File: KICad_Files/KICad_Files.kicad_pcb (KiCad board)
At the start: 2 copper layers, 30 x 34 mm, 42 parts, among them J1 Conn_01x03_MountingPin, J2 Conn_01x03_MountingPin, J3 Conn_01x03_MountingPin, J4 USB_C_Receptacle_USB2.0_14P, J5 Conn_01x06, J6 Conn_01x06, J7 Conn_01x03_Pin, J8 Conn_01x03_Pin, SW1 Reset, SW2 Boot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

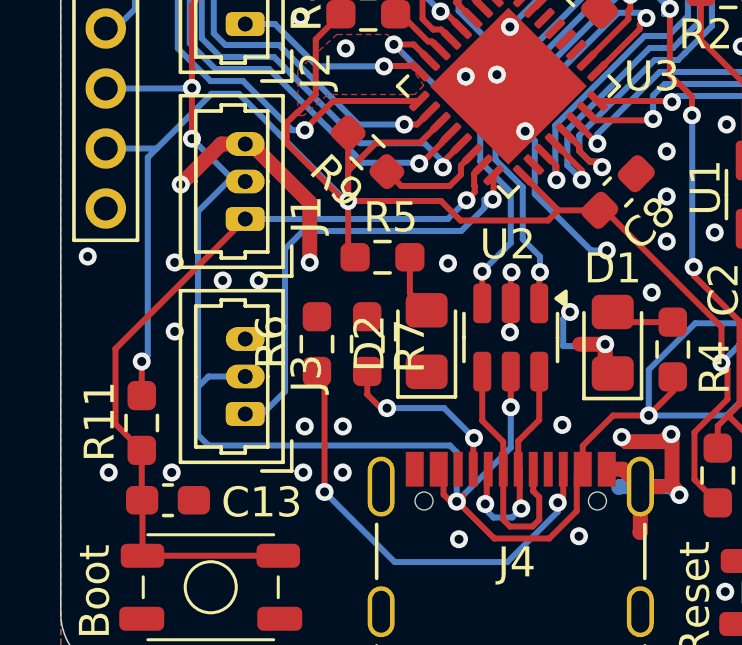
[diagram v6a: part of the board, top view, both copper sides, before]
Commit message: Properly named all I/O Pins/ Power Pins on the Back fixed some minor errors where the silkscreen wasnt aligned properly
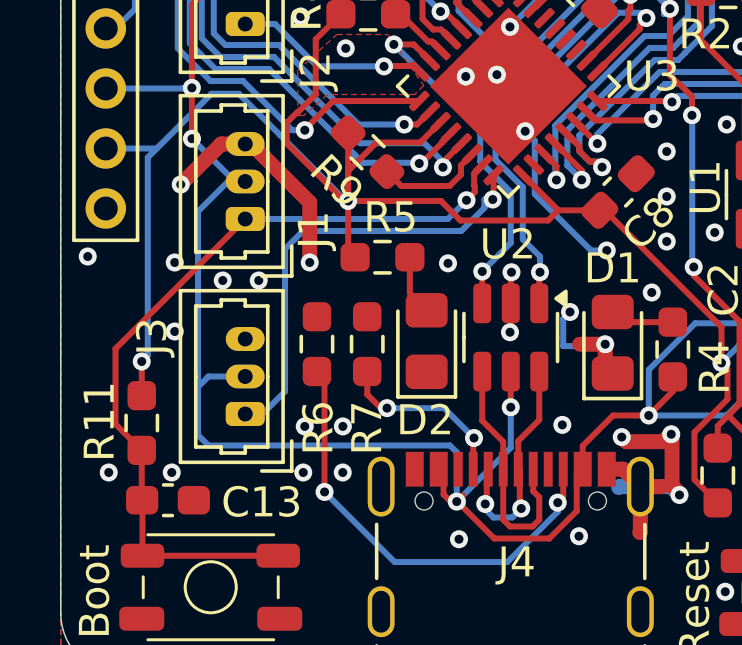
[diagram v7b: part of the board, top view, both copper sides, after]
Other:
- board text added: "3.3V"
- board text added: "GPIO0/4"
- board text added: "GPIO1/5"
- board text added: "GPIO12/19"
- board text added: "GPIO13/20"
- board text added: "GPIO14/21"
- board text added: "GPIO15/22"
- board text added: "GPIO16/23"
- board text added: "GPIO17/24"
- board text added: "GPIO3/8"
- board text added: "GPIO5/10"
- board text added: "GPIO6/12"
- board text added: "GPIO7/13"
- board text added: "GPIO9/15"
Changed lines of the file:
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@@
 		(tags "resistor handsolder")
 		(property "Reference" "R7"
-			(at 0.0625 -1.425 90)
+			(at 2.794 0 90)
 			(layer "F.SilkS")
 			(effects
@@
 		(tags "connector Molex PicoBlade side entry")
 		(property "Reference" "J3"
-			(at 1.35 2.05 90)
+			(at 2.5832 -3.0964 90)
 			(layer "F.SilkS")
 			(effects
@@
 		(tags "connector Molex PicoBlade side entry")
 		(property "Reference" "J1"
-			(at 0.15 2.05 90)
+			(at -0.3608 2.2884 90)
 			(layer "F.SilkS")
 			(effects
@@
 		(tags "LED handsolder")
 		(property "Reference" "D2"
-			(at -0.075 -1.9 90)
+			(at -2.6416 -0.0508 180)
 			(layer "F.SilkS")
 			(effects
@@
 		(tags "resistor handsolder")
 		(property "Reference" "R6"
-			(at -0.075 1.525 90)
+			(at 2.794 -0.0508 90)
 			(layer "F.SilkS")
 			(effects
@@
 		)
 	)
-	(gr_text "GPIO4/9"
-		(at 96.580801 93.616401 -45)
-		(layer "B.SilkS")
-		(effects
-			(font
-				(size 0.5 0.5)
-				(thickness 0.1)
-			)
-			(justify left bottom mirror)
-		)
-	)
-	(gr_text "GPIO4/9"
-		(at 95.869601 81.170401 90)
+	(gr_text "GPIO1/5"
+		(at 96.580801 93.616401 315)
 		(layer "B.SilkS")
 		(effects
@@
 		)
 	)
-	(gr_text "GPIO4/9"
+	(gr_text "GPIO15/22"
 		(at 119.440801 89.247601 45)
 		(layer "B.SilkS")
@@
 	)
 	(gr_text "5V"
-		(at 99.984401 104.843201 0)
+		(at 100.136801 104.843201 0)
 		(layer "B.SilkS")
 		(effects
@@
 		)
 	)
-	(gr_text "GPIO4/9"
-		(at 96.580801 97.629601 -45)
-		(layer "B.SilkS")
-		(effects
-			(font
-				(size 0.5 0.5)
-				(thickness 0.1)
-			)
-			(justify left bottom mirror)
-		)
-	)
-	(gr_text "GPIO4/9"
-		(at 96.580801 91.635201 -45)
+	(gr_text "5V"
+		(at 94.904401 96.156401 315)
 		(layer "B.SilkS")
 		(effects
@@
 	)
 	(gr_text "GPIO4/9"
-		(at 97.901601 81.170401 90)
+		(at 96.580801 91.635201 315)
 		(layer "B.SilkS")
 		(effects
@@
 		)
 	)
-	(gr_text "GPIO4/9"
-		(at 99.374801 89.603201 -45)
+	(gr_text "GPIO6/12"
+		(at 99.527201 89.958801 315)
 		(layer "B.SilkS")
 		(effects
@@
 		)
 	)
-	(gr_text "GPIO4/9"
+	(gr_text "GPIO12/19"
 		(at 114.767201 87.317201 45)
 		(layer "B.SilkS")
@@
 		)
 	)
-	(gr_text "GPIO10/16"
-		(at 103.286401 93.057601 0)
+	(gr_text "GPIO3/8"
+		(at 102.422801 93.057601 0)
 		(layer "B.SilkS")
 		(effects
@@
 		)
 	)
-	(gr_text "GPIO4/9"
-		(at 97.241201 89.603201 -45)
+	(gr_text "GPIO5/10"
+		(at 97.241201 89.603201 315)
 		(layer "B.SilkS")
 		(effects
@@
 		)
 	)
-	(gr_text "GPIO4/9"
+	(gr_text "3.3V"
 		(at 119.440801 97.274001 45)
 		(layer "B.SilkS")
@@
 		)
 	)
-	(gr_text "GPIO4/9"
-		(at 96.580801 101.642801 -45)
+	(gr_text "GND"
+		(at 95.361601 100.677601 315)
 		(layer "B.SilkS")
 		(effects
@@
 		)
 	)
-	(gr_text "GPIO4/9"
+	(gr_text "GPIO14/21"
 		(at 118.729601 87.266401 45)
 		(layer "B.SilkS")
@@
 		)
 	)
-	(gr_text "GPIO4/9"
+	(gr_text "5V"
 		(at 119.440801 95.242001 45)
 		(layer "B.SilkS")
@@
 		)
 	)
-	(gr_text "GPIO4/9"
+	(gr_text "GPIO17/24"
 		(at 119.440801 93.260801 45)
 		(layer "B.SilkS")
@@
 		)
 	)
-	(gr_text "GPIO10/16"
+	(gr_text "GPIO9/15"
 		(at 103.337201 99.560001 0)
 		(layer "B.SilkS")
@@
 		)
 	)
-	(gr_text "GPIO4/9"
+	(gr_text "GND"
 		(at 119.440801 99.255201 45)
 		(layer "B.SilkS")
@@
 		)
 	)
-	(gr_text "GPIO4/9"
-		(at 101.305201 89.552401 -45)
+	(gr_text "GPIO7/13\n"
+		(at 101.660801 90.009601 315)
 		(layer "B.SilkS")
 		(effects
@@
 		)
 	)
-	(gr_text "GPIO4/9"
+	(gr_text "GPIO13/20"
 		(at 116.748401 87.317201 45)
 		(layer "B.SilkS")
@@
 		)
 	)
-	(gr_text "GPIO4/9"
-		(at 96.580801 95.648401 -45)
+	(gr_text "GPIO0/4"
+		(at 96.580801 95.648401 315)
 		(layer "B.SilkS")
 		(effects
@@
 		)
 	)
-	(gr_text "GPIO4/9"
-		(at 96.580801 99.661601 -45)
-		(layer "B.SilkS")
-		(effects
-			(font
-				(size 0.5 0.5)
-				(thickness 0.1)
-			)
-			(justify left bottom mirror)
-		)
-	)
-	(gr_text "GPIO4/9"
-		(at 93.888401 81.170401 90)
+	(gr_text "3.3V"
+		(at 95.412401 98.848801 315)
 		(layer "B.SilkS")
 		(effects
@@
 		)
 	)
-	(gr_text "GPIO4/9"
+	(gr_text "GPIO16/23"
 		(at 119.440801 91.228801 45)
 		(layer "B.SilkS")
@@
 	)
 	(gr_text "5V"
-		(at 100.035201 91.838401 0)
+		(at 100.136801 91.838401 0)
 		(layer "B.SilkS")
 		(effects

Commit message: Fixed Voltage Divider values in PCB Editor
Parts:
- R2: value 10 kΩ -> 68kΩ
- R3: value 220kΩ -> 15kΩ
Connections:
- L1 pad 1: Net-(U1-SW) -> +3.3V
- L1 pad 2: +3.3V -> Net-(U1-SW)
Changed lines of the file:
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@@
 			(layers "F.Cu" "F.Paste" "F.Mask")
 			(roundrect_rratio 0.175439)
-			(net 17 "Net-(U1-SW)")
+			(net 5 "+3.3V")
 			(pinfunction "1")
 			(pintype "passive")
@@
 			(layers "F.Cu" "F.Paste" "F.Mask")
 			(roundrect_rratio 0.175439)
-			(net 5 "+3.3V")
+			(net 17 "Net-(U1-SW)")
 			(pinfunction "2")
 			(pintype "passive")
@@
 			)
 		)
-		(property "Value" "10 kΩ"
+		(property "Value" "68kΩ"
 			(at 0 1.43 0)
 			(layer "F.Fab")
@@
 			)
 		)
-		(property "Value" "220kΩ"
+		(property "Value" "15kΩ"
 			(at 0 1.43 0)
 			(layer "F.Fab")
